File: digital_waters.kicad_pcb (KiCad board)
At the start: 4 copper layers, 188.5 x 82 mm, 113 parts, among them J1 pH_IN, J10 ESP_Only, J11 ESP32 [R], J12 SPI_EXPANSION, J13 I2C_EXPANSION, J14 Calibration_In, J16 ESP32 [L], J17 Atlas Surveyor, J18 EZO Carrier Board, J2 PT-100_TEMP_IN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

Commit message: Added board mounting holes, basic dimensions, and a board pdf file for casual viewing.
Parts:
- added H13: MountingHole, MountingHole:MountingHole_2.7mm_M2.5_ISO14580, F.Cu at (55.0, 46.0)
- added H14: MountingHole, MountingHole:MountingHole_2.7mm_M2.5_ISO14580, F.Cu at (220.0, 46.0)
- added H15: MountingHole, MountingHole:MountingHole_2.7mm_M2.5_ISO14580, F.Cu at (55.0, 122.0)
- added H16: MountingHole, MountingHole:MountingHole_2.7mm_M2.5_ISO14580, F.Cu at (234.0, 108.0)
- added H17: MountingHole, MountingHole:MountingHole_2.7mm_M2.5_ISO14580, F.Cu at (166.0, 122.0)
- moved C46 45.4 mm to (154.9, 64.3)
- moved U6 45.4 mm to (155.5, 97.6)
- moved C33 45.4 mm to (139.6, 97.8)
- moved C34 45.4 mm to (148.3, 97.7)
- moved C35 45.4 mm to (144.3, 97.7)
- moved C48 45.4 mm to (154.9, 60.5)
- moved C6 45.4 mm to (82.3, 92.8)
- moved C95 45.4 mm to (156.2, 90.2)
- moved H3 45.4 mm to (134.3, 49.3)
- moved H4 45.4 mm to (134.3, 73.3)
- moved H5 45.4 mm to (159.3, 49.3)
- moved H6 45.4 mm to (159.3, 73.3)
- moved H7 45.4 mm to (195.8, 49.3)
- moved H8 45.4 mm to (195.8, 73.3)
- moved J10 45.4 mm to (233.8, 57.8)
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
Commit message: Added some silkscreen comments. Added a keepout for the ESP32 antenna.
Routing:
- net /Micocontroller/GPIO_26_PI: track 25.9 -> 29.0 mm
- net /Micocontroller/GPIO_12: track 76.5 -> 74.4 mm
- net /Micocontroller/GPIO_15: track 86.8 -> 84.8 mm
- net /Micocontroller/GPIO_20_PI: track 11.6 -> 13.5 mm
- net /Micocontroller/GPIO_4: track 93.1 -> 91.3 mm
- net /Micocontroller/GPIO_14: track 99.8 -> 98.2 mm
- net /Micocontroller/GPIO_16_PI: track 11.3 -> 12.6 mm
- net /Micocontroller/GPIO_13_PI: track 25.3 -> 24.4 mm
- net /Micocontroller/GPIO_21: track 81.7 -> 82.6 mm
- net /Micocontroller/GPIO_6_PI: track 25.4 -> 24.7 mm
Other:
- board text added: "GNDD +3.3V +5V GPIO_25 GPIO_4 GPIO_14 GPIO_15 GPIO_21 GPIO_12 GPIO_5 GPIO_22 GNDD GNDD GPIO_1"
- board text added: "Insert upsidedown"
- board text added: "MISO GNDD MOSI SCLK"
- board text added: "P1&2 ESP32 P2&3 RPi"
- board text added: "SDA GNDD SCL GNDD"
- board text added: "WMD_Prototype v0.0.1 AZT 20250619"

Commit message: Generated gerbers
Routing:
- net /Micocontroller/GPIO_39_ESP: track 69.5 -> 54.5 mm
- net /Micocontroller/GPIO_19_PI: track 26.7 -> 25.3 mm
- net /Power/+2.5V_REF: track 57.0 -> 55.7 mm
- net GNDA: track 18.4 -> 17.8 mm
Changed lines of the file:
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@@
 			(outputformat 1)
 			(mirror no)
-			(drillshape 1)
+			(drillshape 0)
 			(scaleselection 1)
-			(outputdirectory "")
+			(outputdirectory "/home/atop/Documents/development/other/DigitalWaters/schematics/DigitalWaters_WD_prototype/")
 		)
 	)
@@
 	)
 	(segment
-		(start 59.347325 114.318816)
-		(end 59.747325 114.718816)
-		(width 0.2)
-		(layer "F.Cu")
-		(net 1)
-	)
-	(segment
 		(start 63.947325 66.818816)
 		(end 65.847325 66.818816)
@@
 	)
 	(segment
-		(start 80.847325 81.618816)
-		(end 78.847325 81.618816)
+		(start 76.922325 81.618816)
+		(end 80.847325 81.618816)
 		(width 0.2)
 		(layer "F.Cu")
@@
 	)
 	(segment
-		(start 100.359825 88.968816)
-		(end 101.015781 88.968816)
-		(width 0.2)
-		(layer "F.Cu")
-		(net 2)
-	)
-	(segment
-		(start 78.847325 81.618816)
-		(end 76.922325 81.618816)
-		(width 0.2)
-		(layer "F.Cu")
-		(net 2)
-	)
-	(segment
 		(start 98.647326 88.968816)
 		(end 100.359825 88.968816)
@@
 	)
 	(segment
-		(start 101.015781 87.668816)
-		(end 100.359825 87.668816)
-		(width 0.2)
-		(layer "F.Cu")
-		(net 2)
-	)
-	(segment
 		(start 72.847325 81.718816)
 		(end 72.847325 80.818816)
@@
 	)
 	(segment
-		(start 217.909825 77.088816)
-		(end 217.847325 77.151316)
-		(width 0.2)
-		(layer "F.Cu")
-		(net 4)
-	)
-	(segment
 		(start 235.107325 65.078816)
 		(end 236.587325 65.078816)
@@
 	)
 	(segment
-		(start 78.838486 88.827655)
-		(end 78.777325 88.827655)
-		(width 0.2)
-		(layer "F.Cu")
-		(net 19)
-	)
-	(segment
 		(start 84.847325 87.818816)
 		(end 84.847325 84.818816)
@@
 	)
 	(segment
-		(start 191.512949 95.318816)
-		(end 191.512949 95.48444)
-		(width 0.2)
-		(layer "F.Cu")
-		(net 21)
-	)
-	(segment
 		(start 234.727325 70.698816)
 		(end 236.587325 70.698816)
@@
 	)
 	(segment
-		(start 234.347325 70.088816)
-		(end 234.347325 70.318816)
-		(width 0.2)
-		(layer "In1.Cu")
-		(net 21)
-	)
-	(segment
 		(start 219.347325 80.005973)
 		(end 224.347325 75.005973)
@@
 	)
 	(segment
-		(start 94.212325 101.683816)
-		(end 94.347325 101.818816)
-		(width 0.2)
-		(layer "F.Cu")
-		(net 25)
-	)
-	(segment
 		(start 89.347325 107.318816)
 		(end 90.322324 107.318816)
@@
 	)
 	(segment
-		(start 216.347325 120.318816)
-		(end 216.486723 120.318816)
-		(width 0.2)
-		(layer "F.Cu")
-		(net 35)
-	)
-	(segment
 		(start 146.887325 120.858816)
 		(end 146.347325 120.318816)
@@
 	)
 	(segment
-		(start 144.347325 109.358816)
-		(end 144.387325 109.358816)
-		(width 0.2)
-		(layer "In2.Cu")
-		(net 35)
-	)
-	(segment
 		(start 194.347325 102.318816)
 		(end 164.347325 102.318816)
@@
 	)
 	(segment
-		(start 157.307325 109.358816)
-		(end 144.347325 109.358816)
+		(start 144.347325 109.358816)
+		(end 157.307325 109.358816)
 		(width 0.2)
 		(layer "In2.Cu")
@@
 		(net 36)
 	)
-	(segment
-		(start 199.137024 114.837156)
-		(end 199.428985 114.837156)
-		(width 0.2)
-		(layer "F.Cu")
-		(net 36)
-	)
 	(via
 		(at 152.069402 120.318816)
@@
 	(segment
 		(start 70.847325 117.818816)
-		(end 75.847325 117.818816)
-		(width 0.5)
-		(layer "F.Cu")
-		(net 47)
-	)
-	(segment
-		(start 75.847325 117.818816)
 		(end 76.347325 117.818816)
 		(width 0.5)
@@
 	)
 	(segment
-		(start 74.347325 70.106316)
-		(end 74.259825 70.193816)
-		(width 0.5)
-		(layer "F.Cu")
-		(net 50)
-	)
-	(segment
 		(start 152.347325 97.318816)
 		(end 152.347325 91.318816)
@@
 	)
 	(segment
-		(start 129.347325 102.818816)
-		(end 129.847325 102.818816)
-		(width 0.2)
-		(layer "F.Cu")
-		(net 61)
-	)
-	(segment
 		(start 124.747325 102.818816)
-		(end 129.347325 102.818816)
+		(end 129.847325 102.818816)
 		(width 0.2)
 		(layer "F.Cu")
@@
 		(net 71)
 	)
-	(segment
-		(start 236.403988 55.182153)
-		(end 236.347325 55.238816)
-		(width 0.2)
-		(layer "F.Cu")
-		(net 71)
-	)
-	(segment
-		(start 236.434951 55.182153)
-		(end 236.403988 55.182153)
-		(width 0.2)
-		(layer "F.Cu")
-		(net 71)
-	)
 	(via
 		(at 211.347325 97.318816)
@@
 	)
 	(segment
-		(start 221.347325 56.318816)
-		(end 233.347325 56.318816)
-		(width 0.2)
-		(layer "In1.Cu")
-		(net 71)
-	)
-	(segment
 		(start 220.347325 56.318816)
-		(end 221.347325 56.318816)
+		(end 233.347325 56.318816)
 		(width 0.2)
 		(layer "In1.Cu")
@@
 	)
 	(segment
-		(start 236.403988 57.722153)
-		(end 236.434951 57.722153)
-		(width 0.2)
-		(layer "F.Cu")
-		(net 72)
-	)
-	(segment
-		(start 236.347325 57.778816)
-		(end 236.403988 57.722153)
-		(width 0.2)
-		(layer "F.Cu")
-		(net 72)
-	)
-	(segment
 		(start 234.347325 58.318816)
 		(end 234.887325 57.778816)
@@
 	)
 	(segment
-		(start 221.347325 55.318816)
-		(end 220.347325 55.318816)
+		(start 220.347325 55.318816)
+		(end 227.347325 55.318816)
 		(width 0.2)
 		(layer "In2.Cu")
@@
 	)
 	(segment
-		(start 227.347325 55.318816)
-		(end 221.347325 55.318816)
-		(width 0.2)
-		(layer "In2.Cu")
-		(net 74)
-	)
-	(segment
 		(start 220.347325 55.318816)
 		(end 214.347325 61.318816)
@@
 	)
 	(segment
-		(start 236.434951 60.262153)
-		(end 236.403988 60.262153)
-		(width 0.2)
-		(layer "F.Cu")
-		(net 75)
-	)
-	(segment
 		(start 234.347325 60.318816)
 		(end 236.347325 60.318816)
@@
 		(net 75)
 	)
-	(segment
-		(start 236.403988 60.262153)
-		(end 236.347325 60.318816)
-		(width 0.2)
-		(layer "F.Cu")
-		(net 75)
-	)
 	(via
 		(at 212.347325 86.318816)
@@
 	)
 	(segment
-		(start 233.210662 59.318816)
-		(end 218.347325 59.318816)
+		(start 218.347325 59.318816)
+		(end 233.347325 59.318816)
 		(width 0.2)
 		(layer "In2.Cu")
@@
 	)
 	(segment
-		(start 233.347325 59.318816)
-		(end 218.347325 59.318816)
-		(width 0.2)
-		(layer "In2.Cu")
-		(net 75)
-	)
-	(segment
 		(start 227.347325 60.182153)
 		(end 227.483988 60.318816)
@@
 	)
 	(segment
-		(start 219.983988 60.182153)
-		(end 218.983988 60.182153)
+		(start 218.983988 60.182153)
+		(end 227.347325 60.182153)
 		(width 0.2)
 		(layer "In2.Cu")
@@
 	)
 	(segment
-		(start 227.347325 60.182153)
-		(end 219.983988 60.182153)
-		(width 0.2)
-		(layer "In2.Cu")
-		(net 76)
-	)
-	(segment
 		(start 231.347325 119.318816)
 		(end 231.057644 119.608497)
@@
 	)
 	(segment
-		(start 215.4 105.028508)
-		(end 215.4 106.371491)
-		(width 0.2)
-		(layer "F.Cu")
-		(net 84)
-	)
-	(segment

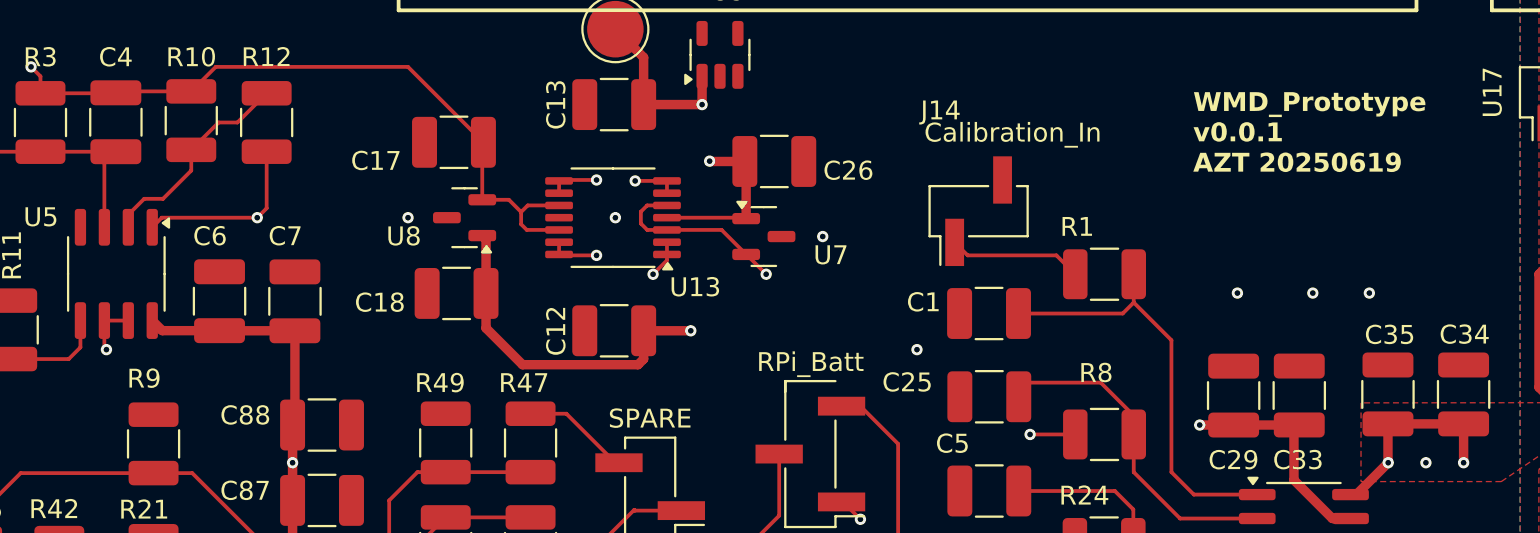
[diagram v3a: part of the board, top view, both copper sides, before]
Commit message: BUG_FIX ------- - Swapped ground for the 2.5V reference on the non-inverting leg of U11B (External temperature probe)   This is due to the fact that the temp probe voltage can go both above and below the reference point so we need something higher than ground to prevent pegging the output to 0 when temp probe impedance drops below 1k.
FEATURES
--------
- Finalized many of the parts for the BOM
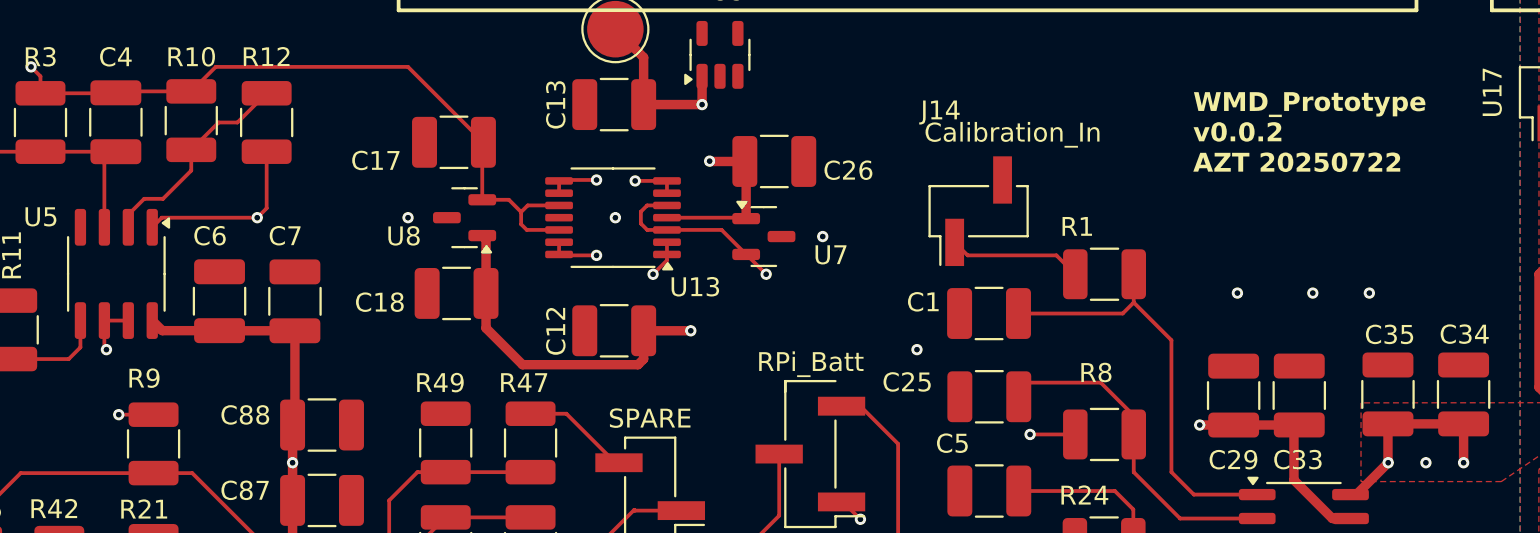
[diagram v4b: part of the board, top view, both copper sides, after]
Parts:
- C1, C2, C23, C24, C25, C3, C5: value C -> 800n
- R1, R19, R20, R24, R50, R51, R8: value R -> 1k
- R21, R9: value R -> 100k
- R42, R46: value R -> 10k
- R47, R7: value R -> 10
- R48, R49: value R -> 200
- R52: value 5k -> 1k
- R6: value R -> 990
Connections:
- C17 pad 1: /Power/+2.5V_REF -> /Base_Sensor/+2.5V_REF
- C4 pad 2: /Power/+2.5V_REF -> /Base_Sensor/+2.5V_REF
- C58 pad 2: /Power/+2.5V_REF -> /Base_Sensor/+2.5V_REF
- R10 pad 1: /Power/+2.5V_REF -> /Base_Sensor/+2.5V_REF
- R11 pad 1: /Power/+2.5V_REF -> /Base_Sensor/+2.5V_REF
- R3 pad 1: /Power/+2.5V_REF -> /Base_Sensor/+2.5V_REF
- R9 pad 1: GNDA -> /Base_Sensor/+2.5V_REF
- U13 pad 10: /Power/+2.5V_REF -> /Base_Sensor/+2.5V_REF
- U13 pad 12: /Power/+2.5V_REF -> /Base_Sensor/+2.5V_REF
- U8 pad 2: /Power/+2.5V_REF -> /Base_Sensor/+2.5V_REF
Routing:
- net /Base_Sensor/+2.5V_REF: track 0.00 -> 70.8 mm, vias 0 -> 3
- net /Power/+2.5V_REF: track 55.7 -> 0.00 mm, vias 2 -> 0
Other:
- board text added: "WMD_Prototype v0.0.2 AZT 20250722"
- board text removed: "WMD_Prototype v0.0.1 AZT 20250619"
